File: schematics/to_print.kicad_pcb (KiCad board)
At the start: 2 copper layers, 165.7 x 122.6 mm, 124 parts, among them IC1 SN754410, J1 POWER, J2 MOT-LEFT, J3 MOT-RIGHT, J4 ICSP, J5 ESP-RS232, J6 MOT-POWER, J7 DEBUG-TX, Q1 BC547, Q2 BC547, SW1 FLASH, SW2 RESET, SW3 RESET, U1 L7805CV, U2 PIC24FJ32GA002-I/SP, U3 LM1117T-3.3, U4 ESP-12E, U5 MPU-92/65_breakout_board

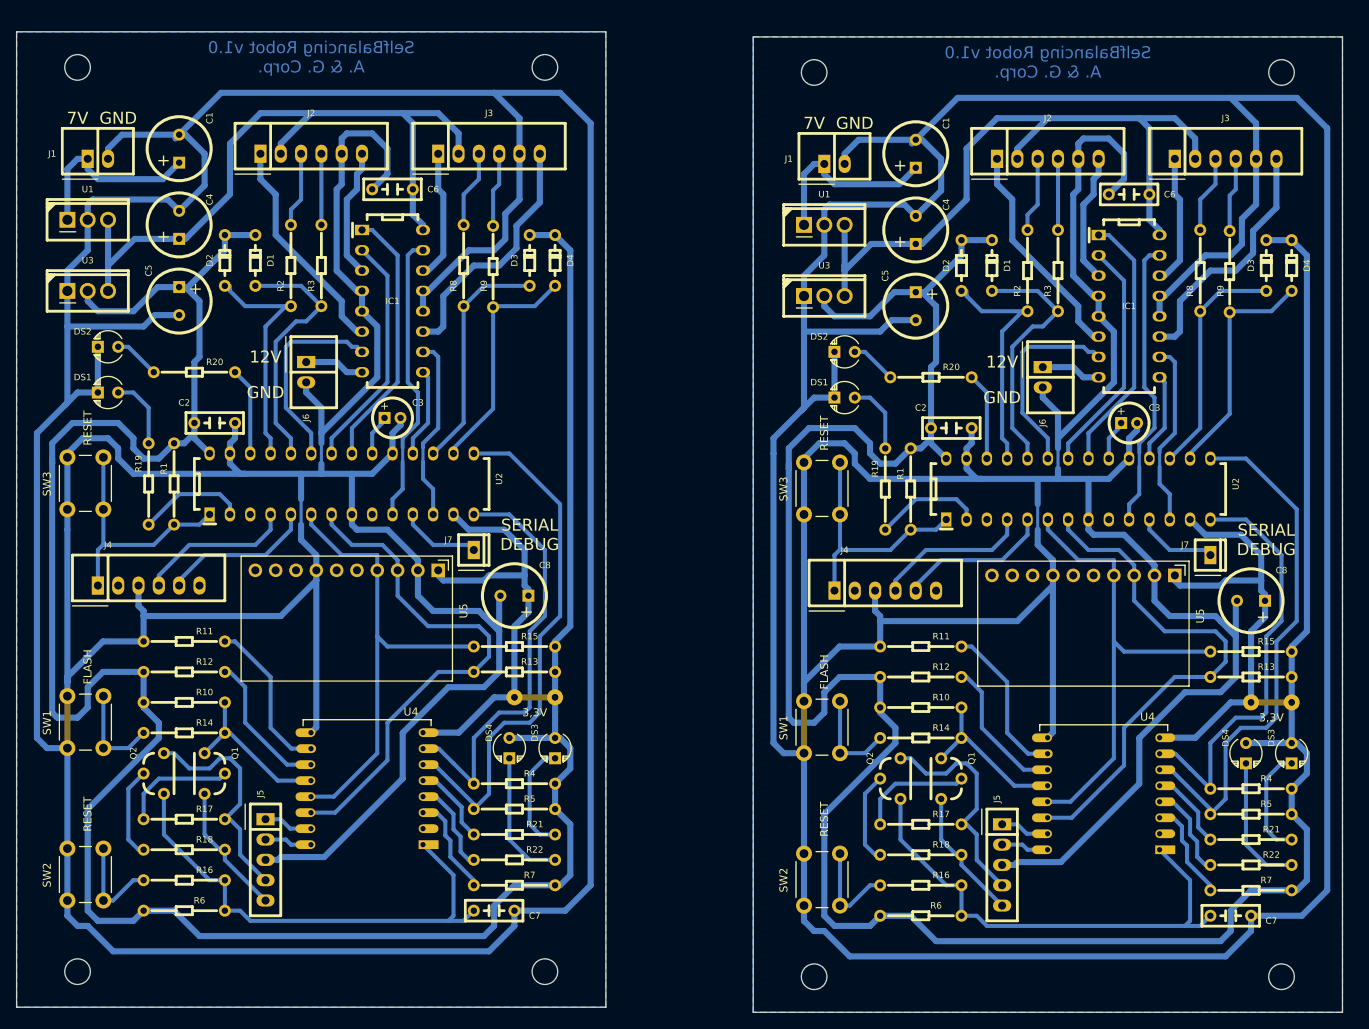
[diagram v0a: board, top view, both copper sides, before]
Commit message: - Mejorada señalización por leds en PIC y ESP8266
- ESP8266: Un error de la conexión a la Wifi permite continuar el programa
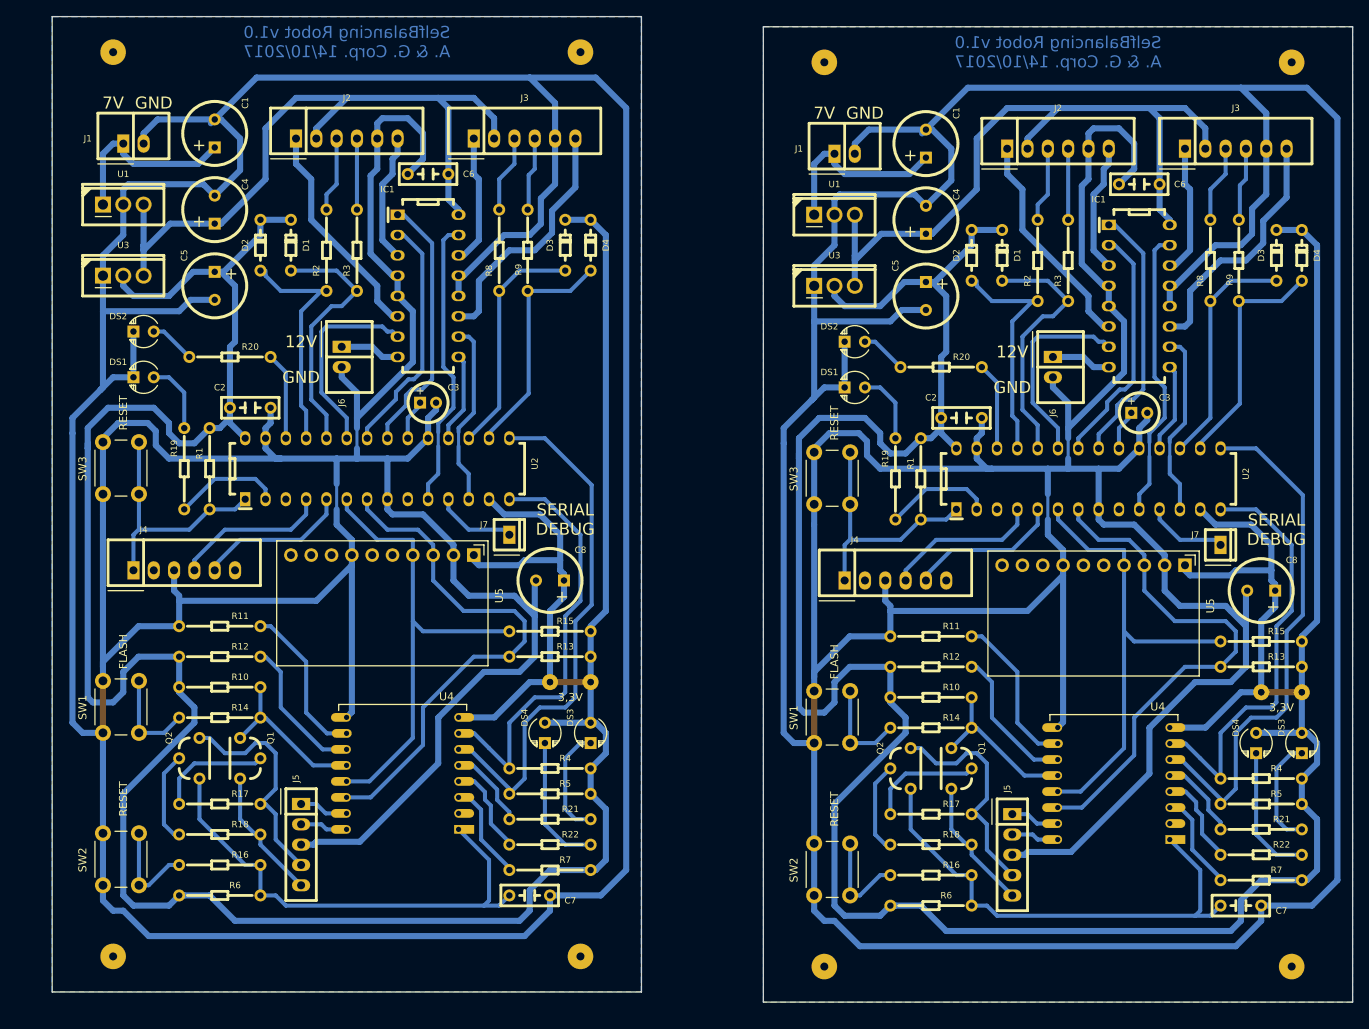
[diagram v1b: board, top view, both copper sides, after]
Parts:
- removed the 3,3V at (87.0, 107.3)
- removed the 3,3V at (179.1, 108.0)
- removed the ? at (81.9, 107.3)
- removed the ? at (174.0, 108.0)
- removed the C1 at (40.0, 38.7)
- removed the C1 at (132.1, 39.4)
- removed the C2 at (44.5, 73.0)
- removed the C2 at (136.5, 73.7)
- removed the C3 at (66.7, 72.4)
- removed the C3 at (158.8, 73.0)
- removed the C4 at (40.0, 48.3)
- removed the C4 at (132.1, 48.9)
- removed the C5 at (40.0, 57.8)
- removed the C5 at (132.1, 58.4)
- removed the C6 at (66.7, 43.8)
- removed the C6 at (158.8, 44.5)
- removed the C7 at (79.4, 134.0)
- removed the C7 at (171.4, 134.6)
- removed the C8 at (81.9, 94.6)
- removed the C8 at (174.0, 95.2)
- removed the D1 at (49.5, 52.7)
- removed the D1 at (141.6, 53.3)
- removed the D2 at (45.7, 52.7)
- removed the D2 at (137.8, 53.3)
- removed the D3 at (83.8, 52.7)
- removed the D3 at (175.9, 53.3)
- removed the D4 at (87.0, 52.7)
- removed the D4 at (179.1, 53.3)
- removed the DS1 at (31.1, 69.2)
- removed the DS1 at (123.2, 69.8)
- removed the DS2 at (31.1, 63.5)
- removed the DS2 at (123.2, 64.1)
- removed the DS3 at (87.0, 113.7)
- removed the DS3 at (179.1, 114.3)
- removed the DS4 at (81.3, 113.7)
- removed the DS4 at (173.4, 114.3)
- removed the IC1 at (66.7, 57.8)
- removed the IC1 at (158.8, 58.4)
- removed the J1 at (29.8, 40.0)
- removed the J1 at (121.9, 40.6)
- removed the J2 at (56.5, 39.4)
- removed the J2 at (148.6, 40.0)
- removed the J3 at (78.7, 39.4)
- removed the J3 at (170.8, 40.0)
- removed the J4 at (36.2, 93.3)
- removed the J4 at (128.3, 94.0)
- removed the J5 at (50.8, 127.6)
- removed the J5 at (142.9, 128.3)
- removed the J6 at (55.9, 66.7)
- removed the J6 at (148.0, 67.3)
- removed the J7 at (76.8, 88.9)
- removed the J7 at (168.9, 89.5)
- removed the Q1 at (43.2, 116.8)
- removed the Q1 at (135.3, 117.5)
- removed the Q2 at (38.1, 116.8)
- removed the Q2 at (130.2, 117.5)
- removed the R1 at (39.4, 80.6)
- removed the R1 at (131.4, 81.3)
- removed the R10 at (40.6, 108.0)
- removed the R10 at (132.7, 108.6)
- removed the R11 at (40.6, 100.3)
- removed the R11 at (132.7, 101.0)
- removed the R12 at (40.6, 104.1)
- removed the R12 at (132.7, 104.8)
- removed the R13 at (81.9, 104.1)
- removed the R13 at (174.0, 104.8)
- removed the R14 at (40.6, 111.8)
- removed the R14 at (132.7, 112.4)
- removed the R15 at (81.9, 101.0)
- removed the R15 at (174.0, 101.6)
- removed the R16 at (40.6, 130.2)
- removed the R16 at (132.7, 130.8)
- removed the R17 at (40.6, 122.6)
- removed the R17 at (132.7, 123.2)
- removed the R18 at (40.6, 126.4)
- removed the R18 at (132.7, 127.0)
- removed the R19 at (36.2, 80.6)
- removed the R19 at (128.3, 81.3)
- removed the R2 at (54.0, 53.3)
- removed the R2 at (146.1, 54.0)
- removed the R20 at (41.9, 66.7)
- removed the R20 at (134.0, 67.3)
- removed the R21 at (81.9, 124.5)
- removed the R21 at (174.0, 125.1)
- removed the R22 at (81.9, 127.6)
- removed the R22 at (174.0, 128.3)
- removed the R3 at (57.8, 53.3)
- removed the R3 at (149.9, 54.0)
- removed the R4 at (81.9, 118.1)
- removed the R4 at (174.0, 118.7)
- removed the R5 at (81.9, 121.3)
- removed the R5 at (174.0, 121.9)
- removed the R6 at (40.6, 134.0)
- removed the R6 at (132.7, 134.6)
- removed the R7 at (81.9, 130.8)
- removed the R7 at (174.0, 131.4)
- removed the R8 at (75.6, 53.3)
- removed the R8 at (167.6, 54.0)
- removed the R9 at (79.2, 53.5)
- removed the R9 at (171.3, 54.1)
- removed the REF** at (85.7, 141.6)
- removed the REF** at (27.3, 141.6)
- removed the REF** at (27.3, 28.6)
- removed the REF** at (85.7, 28.6)
- removed the REF** at (177.8, 142.2)
- removed the REF** at (119.4, 142.2)
- removed the REF** at (119.4, 29.2)
- removed the REF** at (177.8, 29.2)
- removed the SW1 at (26.0, 113.7)
- removed the SW1 at (118.1, 114.3)
- removed the SW2 at (26.0, 132.7)
- removed the SW2 at (118.1, 133.3)
- removed the SW3 at (26.0, 83.8)
- removed the SW3 at (118.1, 84.5)
- removed the U1 at (28.6, 47.6)
- removed the U1 at (120.7, 48.3)
- removed the U2 at (60.3, 80.6)
- removed the U2 at (152.4, 81.3)
- removed the U3 at (28.6, 56.5)
- removed the U3 at (120.7, 57.1)
- removed the U4 at (70.5, 125.7)
- removed the U4 at (162.6, 126.4)
- removed the U5 at (59.7, 96.5)
- removed the U5 at (151.8, 97.2)
- added 3,3V: , Wire_Pads:SolderWirePad_single_0-8mmDrill, F.Cu at (91.4, 105.4)
- added 3,3V: , Wire_Pads:SolderWirePad_single_0-8mmDrill, F.Cu at (180.3, 106.7)
- added ?: , Wire_Pads:SolderWirePad_single_0-8mmDrill, F.Cu at (86.4, 105.4)
- added ?: , Wire_Pads:SolderWirePad_single_0-8mmDrill, F.Cu at (175.3, 106.7)
- added C1: 220u, selfbalancingrobot:C-ALUM-8mm, F.Cu at (44.5, 36.8)
- added C1: 220u, selfbalancingrobot:C-ALUM-8mm, F.Cu at (133.3, 38.1)
- added C2: 100n, selfbalancingrobot:C-FILM-2.5mm, F.Cu at (48.9, 71.1)
- added C2: 100n, selfbalancingrobot:C-FILM-2.5mm, F.Cu at (137.8, 72.4)
- added C3: 10u, selfbalancingrobot:C-ALUM-5mm, F.Cu at (71.1, 70.5)
- added C3: 10u, selfbalancingrobot:C-ALUM-5mm, F.Cu at (160.0, 71.8)
- added C4: 220u, selfbalancingrobot:C-ALUM-8mm, F.Cu at (44.5, 46.4)
- added C4: 220u, selfbalancingrobot:C-ALUM-8mm, F.Cu at (133.3, 47.6)
- added C5: 220u, selfbalancingrobot:C-ALUM-8mm, F.Cu at (44.5, 55.9)
- added C5: 220u, selfbalancingrobot:C-ALUM-8mm, F.Cu at (133.3, 57.1)
- added C6: 100n, selfbalancingrobot:C-FILM-2.5mm, F.Cu at (71.1, 41.9)
- added C6: 100n, selfbalancingrobot:C-FILM-2.5mm, F.Cu at (160.0, 43.2)
- added C7: 100n, selfbalancingrobot:C-FILM-2.5mm, F.Cu at (83.8, 132.1)
- added C7: 100n, selfbalancingrobot:C-FILM-2.5mm, F.Cu at (172.7, 133.3)
- added C8: 220u, selfbalancingrobot:C-ALUM-8mm, F.Cu at (86.4, 92.7)
- added C8: 220u, selfbalancingrobot:C-ALUM-8mm, F.Cu at (175.3, 94.0)
- added D1: 1N4148, selfbalancingrobot:DO-35, F.Cu at (54.0, 50.8)
- added D1: 1N4148, selfbalancingrobot:DO-35, F.Cu at (142.9, 52.1)
- added D2: 1N4148, selfbalancingrobot:DO-35, F.Cu at (50.2, 50.8)
- added D2: 1N4148, selfbalancingrobot:DO-35, F.Cu at (139.1, 52.1)
- added D3: 1N4148, selfbalancingrobot:DO-35, F.Cu at (88.3, 50.8)
- added D3: 1N4148, selfbalancingrobot:DO-35, F.Cu at (177.2, 52.1)
- added D4: 1N4148, selfbalancingrobot:DO-35, F.Cu at (91.4, 50.8)
- added D4: 1N4148, selfbalancingrobot:DO-35, F.Cu at (180.3, 52.1)
- added DS1: IND0, selfbalancingrobot:LED-3mm, F.Cu at (35.6, 67.3)
- added DS1: IND0, selfbalancingrobot:LED-3mm, F.Cu at (124.5, 68.6)
- added DS2: IND1, selfbalancingrobot:LED-3mm, F.Cu at (35.6, 61.6)
- added DS2: IND1, selfbalancingrobot:LED-3mm, F.Cu at (124.5, 62.9)
- added DS3: ESP_IND1, selfbalancingrobot:LED-3mm, F.Cu at (91.4, 111.8)
- added DS3: ESP_IND1, selfbalancingrobot:LED-3mm, F.Cu at (180.3, 113.0)
- added DS4: ESP_IND0, selfbalancingrobot:LED-3mm, F.Cu at (85.7, 111.8)
- added DS4: ESP_IND0, selfbalancingrobot:LED-3mm, F.Cu at (174.6, 113.0)
- added IC1: SN754410, selfbalancingrobot:DIP-16, F.Cu at (71.1, 55.9)
- added IC1: SN754410, selfbalancingrobot:DIP-16, F.Cu at (160.0, 57.1)
- added J1: POWER, selfbalancingrobot:CONN-100MIL-M-1x2-SHROUD, F.Cu at (34.3, 38.1)
- added J1: POWER, selfbalancingrobot:CONN-100MIL-M-1x2-SHROUD, F.Cu at (123.2, 39.4)
- added J2: MOT-LEFT, selfbalancingrobot:CONN-100MIL-M-1x6-SHROUD, F.Cu at (61.0, 37.5)
- added J2: MOT-LEFT, selfbalancingrobot:CONN-100MIL-M-1x6-SHROUD, F.Cu at (149.9, 38.7)
- added J3: MOT-RIGHT, selfbalancingrobot:CONN-100MIL-M-1x6-SHROUD, F.Cu at (83.2, 37.5)
- added J3: MOT-RIGHT, selfbalancingrobot:CONN-100MIL-M-1x6-SHROUD, F.Cu at (172.1, 38.7)
- added J4: ICSP, selfbalancingrobot:CONN-100MIL-M-1x6-SHROUD, F.Cu at (40.6, 91.4)
- added J4: ICSP, selfbalancingrobot:CONN-100MIL-M-1x6-SHROUD, F.Cu at (129.5, 92.7)
- added J5: ESP-RS232, selfbalancingrobot:CONN-100MIL-F-1x5, F.Cu at (55.2, 125.7)
- added J5: ESP-RS232, selfbalancingrobot:CONN-100MIL-F-1x5, F.Cu at (144.1, 127.0)
- added J6: MOT-POWER, selfbalancingrobot:CONN-100MIL-M-1x2-SHROUD, F.Cu at (60.3, 64.8)
- added J6: MOT-POWER, selfbalancingrobot:CONN-100MIL-M-1x2-SHROUD, F.Cu at (149.2, 66.0)
- added J7: DEBUG-TX, selfbalancingrobot:CONN-100MIL-M-1x1, F.Cu at (81.3, 87.0)
- added J7: DEBUG-TX, selfbalancingrobot:CONN-100MIL-M-1x1, F.Cu at (170.2, 88.3)
- added Q1: BC547, selfbalancingrobot:TO-92, F.Cu at (47.6, 114.9)
- added Q1: BC547, selfbalancingrobot:TO-92, F.Cu at (136.5, 116.2)
- added Q2: BC547, selfbalancingrobot:TO-92, F.Cu at (42.5, 114.9)
- added Q2: BC547, selfbalancingrobot:TO-92, F.Cu at (131.4, 116.2)
- added R1: 10K, selfbalancingrobot:R-250mW, F.Cu at (43.8, 78.7)
- added R1: 10K, selfbalancingrobot:R-250mW, F.Cu at (132.7, 80.0)
- added R10: 12K, selfbalancingrobot:R-250mW, F.Cu at (45.1, 106.0)
- added R10: 12K, selfbalancingrobot:R-250mW, F.Cu at (134.0, 107.3)
- added R11: 12K, selfbalancingrobot:R-250mW, F.Cu at (45.1, 98.4)
- added R11: 12K, selfbalancingrobot:R-250mW, F.Cu at (134.0, 99.7)
- added R12: 12K, selfbalancingrobot:R-250mW, F.Cu at (45.1, 102.2)
- added R12: 12K, selfbalancingrobot:R-250mW, F.Cu at (134.0, 103.5)
- added R13: 4K7, selfbalancingrobot:R-250mW, F.Cu at (86.4, 102.2)
- added R13: 4K7, selfbalancingrobot:R-250mW, F.Cu at (175.3, 103.5)
- added R14: 470, selfbalancingrobot:R-250mW, F.Cu at (45.1, 109.9)
- added R14: 470, selfbalancingrobot:R-250mW, F.Cu at (134.0, 111.1)
- added R15: 4K7, selfbalancingrobot:R-250mW, F.Cu at (86.4, 99.1)
- added R15: 4K7, selfbalancingrobot:R-250mW, F.Cu at (175.3, 100.3)
- added R16: 470, selfbalancingrobot:R-250mW, F.Cu at (45.1, 128.3)
- added R16: 470, selfbalancingrobot:R-250mW, F.Cu at (134.0, 129.5)
- added R17: 12K, selfbalancingrobot:R-250mW, F.Cu at (45.1, 120.7)
- added R17: 12K, selfbalancingrobot:R-250mW, F.Cu at (134.0, 121.9)
- added R18: 12K, selfbalancingrobot:R-250mW, F.Cu at (45.1, 124.5)
- added R18: 12K, selfbalancingrobot:R-250mW, F.Cu at (134.0, 125.7)
- added R19: 82, selfbalancingrobot:R-250mW, F.Cu at (40.6, 78.7)
- added R19: 82, selfbalancingrobot:R-250mW, F.Cu at (129.5, 80.0)
- added R2: 1K, selfbalancingrobot:R-250mW, F.Cu at (58.4, 51.4)
- added R2: 1K, selfbalancingrobot:R-250mW, F.Cu at (147.3, 52.7)
- added R20: 82, selfbalancingrobot:R-250mW, F.Cu at (46.4, 64.8)
- added R20: 82, selfbalancingrobot:R-250mW, F.Cu at (135.3, 66.0)
- added R21: 82, selfbalancingrobot:R-250mW, F.Cu at (86.4, 122.6)
- added R21: 82, selfbalancingrobot:R-250mW, F.Cu at (175.3, 123.8)
- added R22: 82, selfbalancingrobot:R-250mW, F.Cu at (86.4, 125.7)
- added R22: 82, selfbalancingrobot:R-250mW, F.Cu at (175.3, 127.0)
- added R3: 1K, selfbalancingrobot:R-250mW, F.Cu at (62.2, 51.4)
- added R3: 1K, selfbalancingrobot:R-250mW, F.Cu at (151.1, 52.7)
- added R4: 4K7, selfbalancingrobot:R-250mW, F.Cu at (86.4, 116.2)
- added R4: 4K7, selfbalancingrobot:R-250mW, F.Cu at (175.3, 117.5)
- added R5: 4K7, selfbalancingrobot:R-250mW, F.Cu at (86.4, 119.4)
- added R5: 4K7, selfbalancingrobot:R-250mW, F.Cu at (175.3, 120.7)
- added R6: 12K, selfbalancingrobot:R-250mW, F.Cu at (45.1, 132.1)
- added R6: 12K, selfbalancingrobot:R-250mW, F.Cu at (134.0, 133.3)
- added R7: 12K, selfbalancingrobot:R-250mW, F.Cu at (86.4, 128.9)
- added R7: 12K, selfbalancingrobot:R-250mW, F.Cu at (175.3, 130.2)
- added R8: 1K, selfbalancingrobot:R-250mW, F.Cu at (80.0, 51.4)
- added R8: 1K, selfbalancingrobot:R-250mW, F.Cu at (168.9, 52.7)
- added R9: 1K, selfbalancingrobot:R-250mW, F.Cu at (83.6, 51.4)
- added R9: 1K, selfbalancingrobot:R-250mW, F.Cu at (172.5, 52.7)
- added REF**: MountingHole_3.2mm_M3, Mounting_Holes:MountingHole_3.2mm_M3, F.Cu at (90.2, 139.7)
- added REF**: MountingHole_3.2mm_M3, Mounting_Holes:MountingHole_3.2mm_M3, F.Cu at (31.8, 139.7)
- added REF**: MountingHole_3.2mm_M3, Mounting_Holes:MountingHole_3.2mm_M3, F.Cu at (31.8, 26.7)
- added REF**: MountingHole_3.2mm_M3, Mounting_Holes:MountingHole_3.2mm_M3, F.Cu at (90.2, 26.7)
- added REF**: MountingHole_3.2mm_M3, Mounting_Holes:MountingHole_3.2mm_M3, F.Cu at (179.1, 141.0)
- added REF**: MountingHole_3.2mm_M3, Mounting_Holes:MountingHole_3.2mm_M3, F.Cu at (120.7, 141.0)
- added REF**: MountingHole_3.2mm_M3, Mounting_Holes:MountingHole_3.2mm_M3, F.Cu at (120.7, 27.9)
- added REF**: MountingHole_3.2mm_M3, Mounting_Holes:MountingHole_3.2mm_M3, F.Cu at (179.1, 27.9)
- added SW1: FLASH, selfbalancingrobot:SW_PUSH_6mm_h5mm, F.Cu at (30.5, 111.8)
- added SW1: FLASH, selfbalancingrobot:SW_PUSH_6mm_h5mm, F.Cu at (119.4, 113.0)
- added SW2: RESET, selfbalancingrobot:SW_PUSH_6mm_h5mm, F.Cu at (30.5, 130.8)
- added SW2: RESET, selfbalancingrobot:SW_PUSH_6mm_h5mm, F.Cu at (119.4, 132.1)
- added SW3: RESET, selfbalancingrobot:SW_PUSH_6mm_h5mm, F.Cu at (30.5, 81.9)
- added SW3: RESET, selfbalancingrobot:SW_PUSH_6mm_h5mm, F.Cu at (119.4, 83.2)
- added U1: L7805CV, selfbalancingrobot:TO-220, F.Cu at (33.0, 45.7)
- added U1: L7805CV, selfbalancingrobot:TO-220, F.Cu at (121.9, 47.0)
- added U2: PIC24FJ32GA002-I/SP, selfbalancingrobot:DIP-28, F.Cu at (64.8, 78.7)
- added U2: PIC24FJ32GA002-I/SP, selfbalancingrobot:DIP-28, F.Cu at (153.7, 80.0)
- added U3: LM1117T-3.3, selfbalancingrobot:TO-220, F.Cu at (33.0, 54.6)
- added U3: LM1117T-3.3, selfbalancingrobot:TO-220, F.Cu at (121.9, 55.9)
- added U4: ESP-12E, selfbalancingrobot:ESP-12, F.Cu at (74.9, 123.8)
- added U4: ESP-12E, selfbalancingrobot:ESP-12, F.Cu at (163.8, 125.1)
- added U5: MPU-92/65_breakout_board, selfbalancingrobot:MPU9265_breakout, F.Cu at (64.1, 94.6)
- added U5: MPU-92/65_breakout_board, selfbalancingrobot:MPU9265_breakout, F.Cu at (153.0, 95.9)
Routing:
- net Net-(R21-Pad2): track 25.3 -> 28.7 mm
- net Net-(R22-Pad2): track 23.7 -> 26.6 mm
- net /MOT_LEFT_DIR0: track 60.5 -> 62.0 mm
- net GND: track 1478.2 -> 1479.2 mm
- net /MOT_SCL: track 133.8 -> 132.9 mm
- net /MOT_LEFT_PWM: track 65.8 -> 66.5 mm
- net Net-(R7-Pad2): track 28.9 -> 28.4 mm
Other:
- board size 165.7 x 122.6 mm -> 162.6 x 123.2 mm
- net class Default: clearance 0.381 -> 0.508
- net class Power: clearance 0.381 -> 0.508
- rule trace_clearance: 0.381 -> 0.508
- board text added: "SelfBalancing Robot v1.0 A. & G. Corp. 14/10/2017"
- board text removed: "SelfBalancing Robot v1.0 A. & G. Corp."
